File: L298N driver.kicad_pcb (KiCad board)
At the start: 2 copper layers, 132.8 x 80 mm, 39 parts, among them J1 Screw_Terminal_01x03, J2 Conn_01x02_Pin, J3 Conn_01x05, J4 Conn_01x05, J5 Conn_01x02, J6 Conn_01x02, J7 Conn_01x02, J8 Conn_01x02, U1 74HC595, U2 LM78M05_TO220, U3 DEV-15795, U4 L298N, U5 L298N

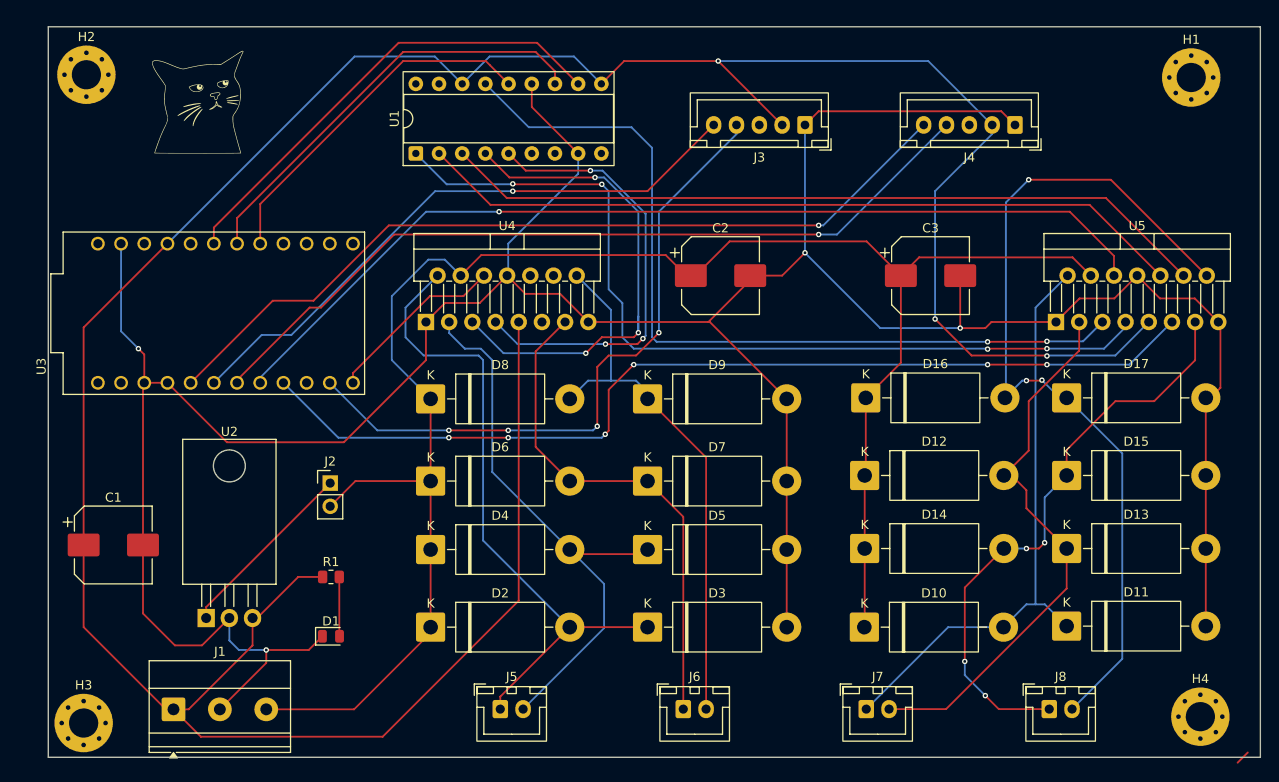
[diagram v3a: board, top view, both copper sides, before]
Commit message: rounded corners
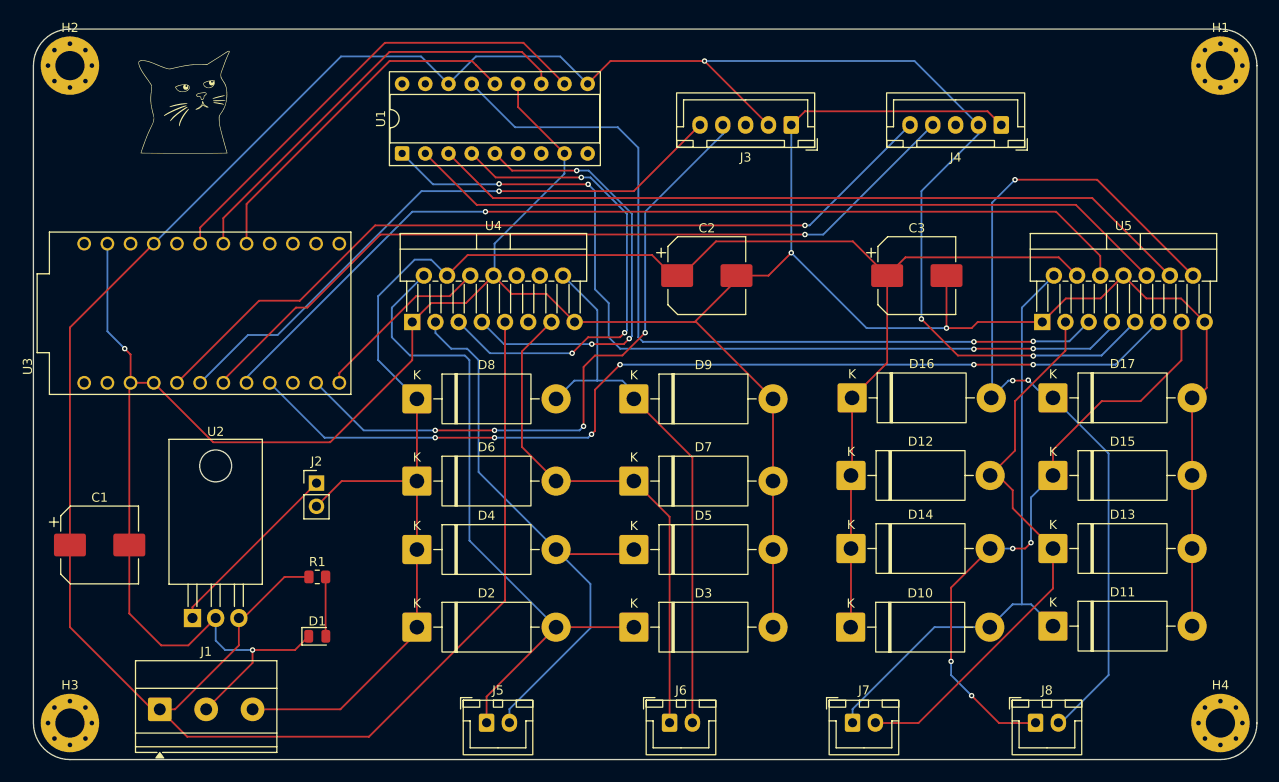
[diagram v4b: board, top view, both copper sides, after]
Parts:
- moved H1 3.45 mm to (198.0, 72.0)
- moved H4 2.30 mm to (198.0, 144.0)
- moved J5 2.11 mm to (117.6, 144.0)
- moved J6 2.11 mm to (137.7, 144.0)
- moved J7 2.11 mm to (157.7, 144.0)
- moved J8 2.11 mm to (177.8, 144.0)
- moved H2 2.06 mm to (72.0, 72.0)
- moved C1 1.50 mm to (75.2, 124.5)
- moved C2 1.50 mm to (141.8, 95.0)
- moved C3 1.50 mm to (164.8, 95.0)
- moved D1 1.50 mm to (99.1, 134.5)
- moved D10 1.50 mm to (157.5, 133.5)
- moved D11 1.50 mm to (179.7, 133.4)
- moved D12 1.50 mm to (157.5, 116.9)
- moved D13 1.50 mm to (179.7, 124.9)
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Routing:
- net Net-(D16-A): track 97.7 -> 99.4 mm
- net (no net): track 1.59 -> 0.00 mm
- net /extraction_in1: track 54.9 -> 53.4 mm
- net Net-(D8-A): track 60.3 -> 61.8 mm
- net Net-(D6-A): track 55.6 -> 57.1 mm
- net Net-(D4-A): track 62.9 -> 64.3 mm
- net Net-(D2-A): track 71.6 -> 73.1 mm
- net Net-(D10-A): track 65.1 -> 66.6 mm
- net Net-(D14-A): track 64.8 -> 65.5 mm
- net Net-(D12-A): track 60.9 -> 61.5 mm
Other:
- board size 132.8 x 80 mm -> 134 x 80 mm

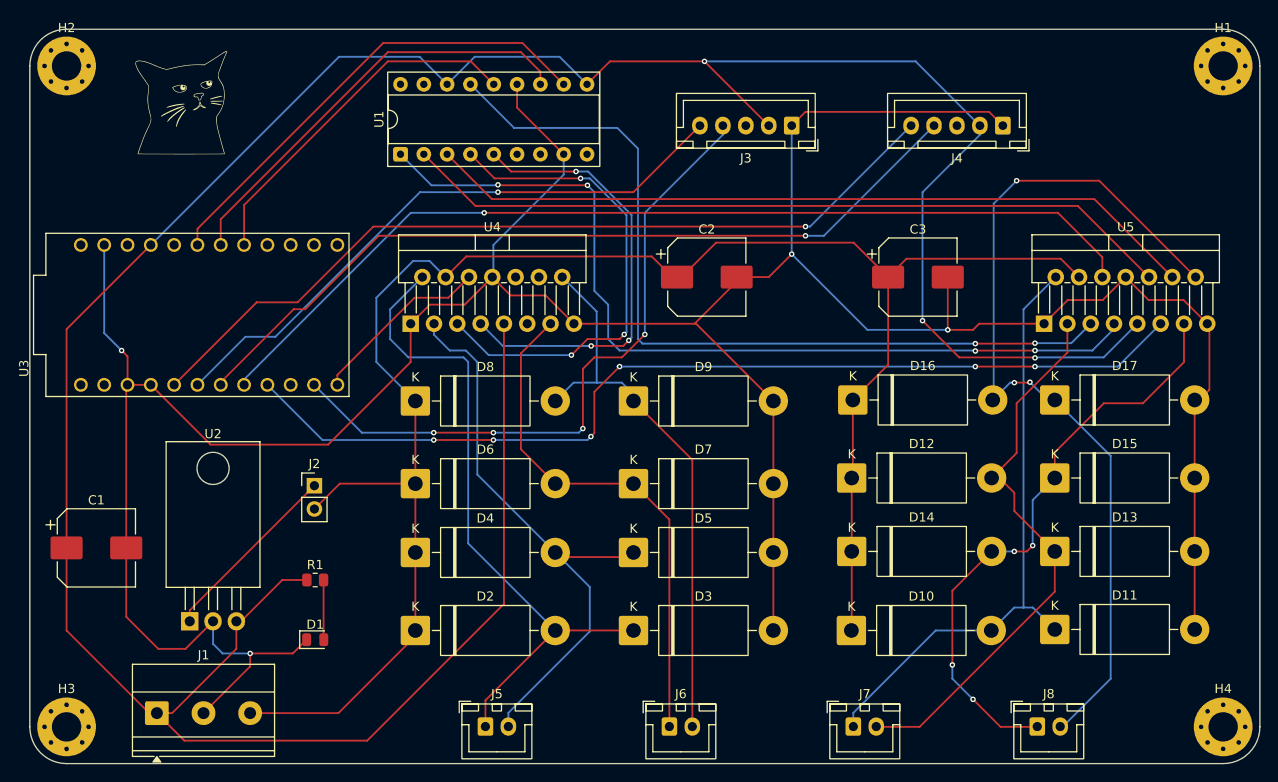
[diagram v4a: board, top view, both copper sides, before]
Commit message: fat traces for 12v and L298N out
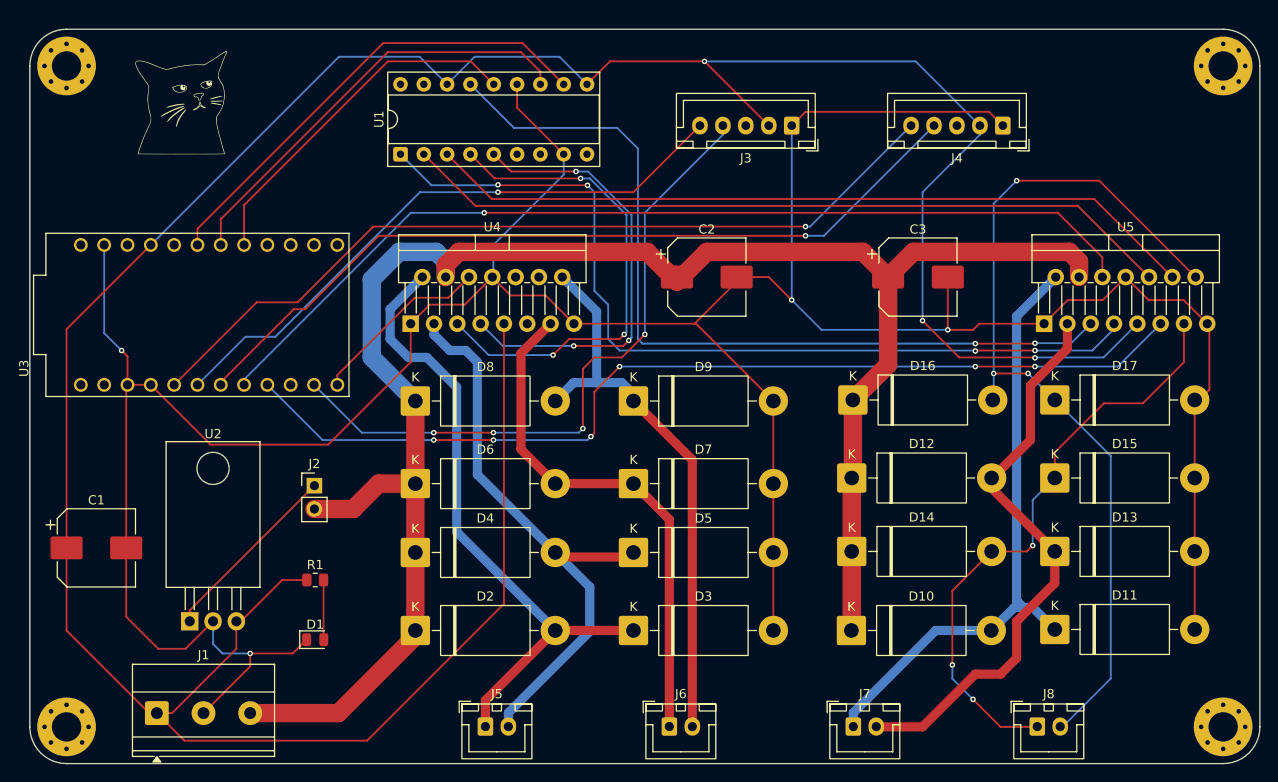
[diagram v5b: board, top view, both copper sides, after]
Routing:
- net VCC: track 197.9 -> 203.6 mm
- net GND: track 362.8 -> 365.7 mm
- net Net-(D2-A): track 73.1 -> 70.7 mm
- net Net-(D12-A): track 61.5 -> 62.9 mm
- net Net-(D16-A): track 99.4 -> 100.7 mm
- net Net-(D10-A): track 66.6 -> 67.3 mm
- net Net-(D14-A): vias 4 -> 3

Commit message: silkscreen labels
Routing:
- net GND: track 365.7 -> 366.8 mm
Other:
- board text added: "+12V"
- board text added: "+5V"
- board text added: "5V regulator En"
- board text added: "Extraction"
- board text added: "GND"
- board text added: "Hydration"
- board text added: "Hydration Speed"
- board text added: "Roller"
- board text added: "Roller Speed"
- board text added: "Sparkfun pro micro 5V/16MHz or its arduino clone ATmega32U4"
- board text added: "Unused"
- board text added: "afiq rosli jan 2026"
- board text added: "v1.0"
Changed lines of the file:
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@@
 		(property "Value" "220uF"
 			(at 0 5.2 0)
-			(layer "F.Fab")
+			(layer "F.SilkS")
 			(effects
 				(font
@@
 		(property "Value" "L298N"
 			(at 8.89 1.85 0)
-			(layer "F.Fab")
+			(layer "F.SilkS")
 			(effects
 				(font
@@
 		(property "Value" "220uF"
 			(at 0 5.2 0)
-			(layer "F.Fab")
+			(layer "F.SilkS")
 			(effects
 				(font
@@
 		)
 		(property "Value" "Conn_01x05"
-			(at 0.75 -2.45 0)
+			(at 4.75 5 0)
 			(layer "F.Fab")
 			(effects
@@
 		(property "Value" "220uF"
 			(at 0 5.2 0)
-			(layer "F.Fab")
+			(layer "F.SilkS")
 			(effects
 				(font
@@
 		(tags "THT Terminal Block Phoenix MKDS-1,5-3-5.08 pitch 5.08mm size 15.2x9.8mm drill 1.3mm pad 2.6mm")
 		(property "Reference" "J1"
-			(at 5.08 -6.32 0)
+			(at -4.09 0 0)
 			(layer "F.SilkS")
 			(effects
@@
 		(property "Value" "L298N"
 			(at 8.89 1.85 0)
-			(layer "F.Fab")
+			(layer "F.SilkS")
 			(effects
 				(font
@@
 		(property "Value" "74HC595"
 			(at 3.81 22.65 90)
-			(layer "F.Fab")
+			(layer "F.SilkS")
 			(effects
 				(font
@@
 		(layer "Edge.Cuts")
 	)
+	(gr_text "GND"
+		(at 85.5 136.75 0)
+		(layer "F.SilkS")
+		(effects
+			(font
+				(size 1 1)
+				(thickness 0.1)
+			)
+			(justify left bottom)
+		)
+	)
+	(gr_text "+5V"
+		(at 80 136.75 0)
+		(layer "F.SilkS")
+		(effects
+			(font
+				(size 1 1)
+				(thickness 0.1)
+			)
+			(justify left bottom)
+		)
+	)
+	(gr_text "afiq rosli\njan 2026"
+		(at 81.25 85.25 0)
+		(layer "F.SilkS")
+		(effects
+			(font
+				(size 1 1)
+				(thickness 0.1)
+			)
+			(justify left bottom)
+		)
+	)
+	(gr_text "Hydration Speed"
+		(at 163.75 84 0)
+		(layer "F.SilkS")
+		(effects
+			(font
+				(size 1 1)
+				(thickness 0.15)
+			)
+			(justify left bottom)
+		)
+	)
+	(gr_text "v1.0"
+		(at 83.545914 80.75 0)
+		(layer "F.SilkS")
+		(effects
+			(font
+				(size 1 1)
+				(thickness 0.1)
+			)
+			(justify left bottom)
+		)
+	)
+	(gr_text "Sparkfun pro micro 5V/16MHz\nor its arduino clone\nATmega32U4"
+		(at 75.5 101.75 0)
+		(layer "F.SilkS")
+		(effects
+			(font
+				(size 1 1)
+				(thickness 0.1)
+			)
+			(justify left bottom)
+		)
+	)
+	(gr_text "+12V"
+		(at 90 136.75 0)
+		(layer "F.SilkS")
+		(effects
+			(font
+				(size 1 1)
+				(thickness 0.1)
+			)
+			(justify left bottom)
+		)
+	)
+	(gr_text "Hydration"
+		(at 174 147.25 90)
+		(layer "F.SilkS")
+		(effects
+			(font
+				(size 1 1)
+				(thickness 0.15)
+			)
+			(justify left bottom)
+		)
+	)
+	(gr_text "Roller Speed"
+		(at 141 84 0)
+		(layer "F.SilkS")
+		(effects
+			(font
+				(size 1 1)
+				(thickness 0.15)
+			)
+			(justify left bottom)
+		)
+	)
+	(gr_text "Unused"
+		(at 134.25 147.5 90)
+		(layer "F.SilkS")
+		(effects
+			(font
+				(size 1 1)
+				(thickness 0.15)
+			)
+			(justify left bottom)
+		)
+	)
+	(gr_text "Roller"
+		(at 154 147 90)
+		(layer "F.SilkS")
+		(effects
+			(font
+				(size 1 1)
+				(thickness 0.15)
+			)
+			(justify left bottom)
+		)
+	)
+	(gr_text "Extraction"
+		(at 114 147.5 90)
+		(layer "F.SilkS")
+		(effects
+			(font
+				(size 1 1)
+				(thickness 0.15)
+			)
+			(justify left bottom)
+		)
+	)
+	(gr_text "5V regulator En"
+		(at 96 125 90)
+		(layer "F.SilkS")
+		(effects
+			(font
+				(size 1 1)
+				(thickness 0.1)
+			)
+			(justify left bottom)
+		)
+	)
 	(segment
 		(start 110 117.5)
@@
 	)
 	(segment
-		(start 98.15 134.5)
-		(end 96.65 136)
-		(width 0.2)
-		(layer "F.Cu")
-		(net 2)
-	)
-	(segment
 		(start 152.5 77)
 		(end 151 78.5)
@@
 	)
 	(segment
-		(start 96.65 136)
-		(end 92 136)
-		(width 0.2)
-		(layer "F.Cu")
-		(net 2)
-	)
-	(segment
 		(start 194.39812 124.768144)
 		(end 194.27812 124.888144)
@@
 	)
 	(segment
+		(start 87.25 142.5)
+		(end 86.92 142.5)
+		(width 0.2)
+		(layer "F.Cu")
+		(net 2)
+	)
+	(segment
 		(start 149 108.5)
 		(end 140.58 100.08)
@@
 	)
 	(segment
+		(start 95.25 134.5)
+		(end 87.25 142.5)
+		(width 0.2)
+		(layer "F.Cu")
+		(net 2)
+	)
+	(segment
 		(start 78.5 124.5)
 		(end 78.5 106.88)
@@
 	)
 	(segment
-		(start 86.92 142.5)
-		(end 92 137.42)
-		(width 0.2)
-		(layer "F.Cu")
-		(net 2)
-	)
-	(segment
 		(start 84.96 135.5)
 		(end 82 135.5)
@@
 	)
 	(segment
+		(start 95.25 134.5)
+		(end 98.15 134.5)
+		(width 0.2)
+		(layer "F.Cu")
+		(net 2)
+	)
+	(segment
 		(start 149 125)
 		(end 149 133.5)
@@
 	)
 	(segment
-		(start 92 137.42)
-		(end 92 136)
-		(width 0.2)
-		(layer "F.Cu")
-		(net 2)
-	)
-	(segment
 		(start 151 97.5)
 		(end 148.5 95)
@@
 	)
 	(via
-		(at 92 136)
+		(at 95.25 134.5)
 		(size 0.6)
 		(drill 0.3)
@@
 	)
 	(segment
-		(start 89 136)
-		(end 87.96 134.96)
-		(width 0.2)
-		(layer "B.Cu")
-		(net 2)
-	)
-	(segment
 		(start 126.16 83.84)
 		(end 126.16 81.62)
@@
 	)
 	(segment
-		(start 92 136)
-		(end 89 136)
-		(width 0.2)
-		(layer "B.Cu")
-		(net 2)
-	)
-	(segment
 		(start 118.38 95)
 		(end 118.5 94.88)
@@
 	)
 	(segment
+		(start 88 132.54)
+		(end 87.96 132.5)
+		(width 0.2)
+		(layer "B.Cu")
+		(net 2)
+	)
+	(segment
+		(start 95.25 134.5)
+		(end 88.75 134.5)
+		(width 0.2)
+		(layer "B.Cu")
+		(net 2)
+	)
+	(segment
 		(start 154.25 100.75)
 		(end 168 100.75)
@@
 	)
 	(segment
-		(start 87.96 134.96)
+		(start 87.96 133.71)
 		(end 87.96 132.5)
 		(width 0.2)
 		(layer "B.Cu")
+		(net 2)
+	)
+	(segment
+		(start 88.75 134.5)
+		(end 87.96 133.71)
+		(width 0.2)
+		(layer "B.Cu")

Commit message: copper pour
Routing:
- added copper zone on B.Cu, net GND
- added copper zone on F.Cu, net GND
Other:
- board text added: "Motor Driver for X996 Mangle Test Rig"
- board text added: "[DT CLK XX 5V GND]"
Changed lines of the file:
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@@
 		(layer "Edge.Cuts")
+	)
+	(gr_text "[DT CLK XX 5V GND]"
+		(at 138.25 72.75 0)
+		(layer "F.SilkS")
+		(effects
+			(font
+				(size 1 1)
+				(thickness 0.1)
+			)
+			(justify left bottom)
+		)
 	)
 	(gr_text "GND"
@@
 		)
 	)
+	(gr_text "Motor Driver for X996 Mangle Test Rig"
+		(at 200.25 124.888144 90)
+		(layer "F.SilkS")
+		(effects
+			(font
+				(size 1 1)
+				(thickness 0.1)
+			)
+			(justify left bottom)
+		)
+	)
 	(gr_text "afiq rosli\njan 2026"
 		(at 81.25 85.25 0)
@@
 		)
 	)
+	(gr_text "[DT CLK XX 5V GND]"
+		(at 161.25 72.75 0)
+		(layer "F.SilkS")
+		(effects
+			(font
+				(size 1 1)
+				(thickness 0.1)
+			)
+			(justify left bottom)
+		)
+	)
 	(gr_text "Sparkfun pro micro 5V/16MHz\nor its arduino clone\nATmega32U4"
 		(at 75.5 101.75 0)
@@
 		(net 40)
 	)
+	(zone
+		(net 2)
+		(net_name "GND")
+		(layers "F.Cu" "B.Cu")
+		(hatch edge 0.5)
+		(connect_pads
+			(clearance 0.5)
+		)
+		(min_thickness 0.25)
+		(filled_areas_thickness no)
+		(fill yes
+			(thermal_gap 0.5)
+			(thermal_bridge_width 0.5)
+		)
+		(polygon
+			(pts
+				(xy 68 68) (xy 68 148) (xy 202 148) (xy 202 68)
+			)
+		)
+	)
 	(embedded_fonts no)

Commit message: initial component layout and smd diode
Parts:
- D10, D11, D12, D13, D14, D15, D16, D17, D2, D3, D4, D5, D6, D7, D8, D9: value UF5401 -> SS34; footprint Diode_THT:D_DO-201AD_P15.24mm_Horizontal -> Diode_SMD:D_SMA
- moved D11 65.4 mm to (136.6, 84.1), turned to 90 degrees
- moved D13 62.9 mm to (131.8, 84.1), turned to 90 degrees
- moved D17 62.7 mm to (121.8, 84.2), turned to 90 degrees
- moved D15 62.2 mm to (126.8, 84.1), turned to 90 degrees
- moved U5 62.0 mm to (116.6, 97.5), turned to 90 degrees
- moved H1 60.0 mm to (138.0, 73.0)
- moved H4 59.1 mm to (139.0, 140.0)
- moved J3 54.3 mm to (97.0, 73.2)
- moved J8 50.4 mm to (127.5, 139.5)
- moved J4 46.8 mm to (127.5, 73.2)
- moved D10 45.1 mm to (136.8, 93.5), turned to 90 degrees
- moved D14 40.6 mm to (131.8, 93.5), turned to 90 degrees
- moved C1 40.0 mm to (111.0, 106.5), turned to -90 degrees
- moved J7 39.7 mm to (118.2, 139.5)
- moved D16 38.9 mm to (121.8, 93.5), turned to 90 degrees
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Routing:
- net VCC: track 203.6 -> 565.9 mm, vias 0 -> 14
- net GND: track 366.8 -> 712.9 mm, vias 4 -> 6
- net Net-(D16-A): track 100.7 -> 230.8 mm
- net +5V: track 326.0 -> 211.1 mm, vias 3 -> 0
- net /hydration_En: track 108.2 -> 0.00 mm, vias 6 -> 0
- net unconnected-(U3-MISO-PadJ4_10): track 0.00 -> 105.8 mm, vias 0 -> 1
- net /roller_En: track 105.8 -> 0.00 mm, vias 1 -> 0
- net /roller_in1: track 92.3 -> 0.00 mm, vias 2 -> 0
- net /hydration_in4: track 84.5 -> 0.00 mm
- net /hydration_in3: track 84.5 -> 0.00 mm
- net /rotary_enc_roller_dt: track 72.7 -> 0.00 mm, vias 4 -> 0
- net Net-(D2-A): track 70.7 -> 0.00 mm
- net /clk: track 51.9 -> 0.00 mm
- net /extraction_in2: track 48.9 -> 0.00 mm, vias 3 -> 0
- net Net-(D6-A): track 57.1 -> 8.73 mm
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- removed copper zone on B.Cu, net GND
- removed copper zone on F.Cu, net GND
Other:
- board size 134 x 80 mm -> 75 x 75 mm
